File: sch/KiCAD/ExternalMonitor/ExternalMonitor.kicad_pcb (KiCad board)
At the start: 2 copper layers, 78.6 x 60.3 mm, 29 parts, among them J1 Conn_01x02_Male, J10 Conn_01x04_Female, J11 Conn_01x08_Female, J12 Conn_01x04_Female, J13 Conn_01x15, J14 Conn_01x03_Pin, J2 Conn_01x02_Male, J3 Conn_01x03_Male, J4 Conn_01x03_Male, J5 Conn_01x03_Female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

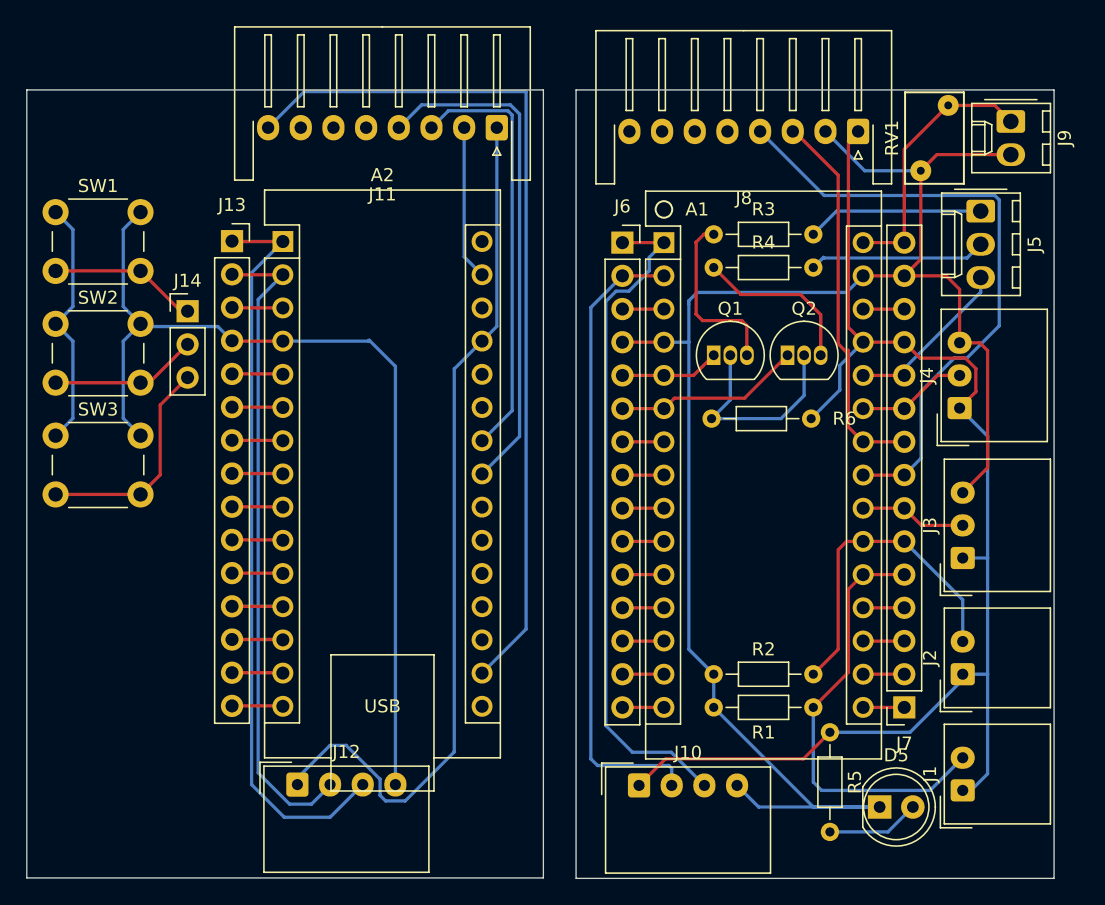
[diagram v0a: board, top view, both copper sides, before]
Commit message: 複製した回路図の重複部分を削除
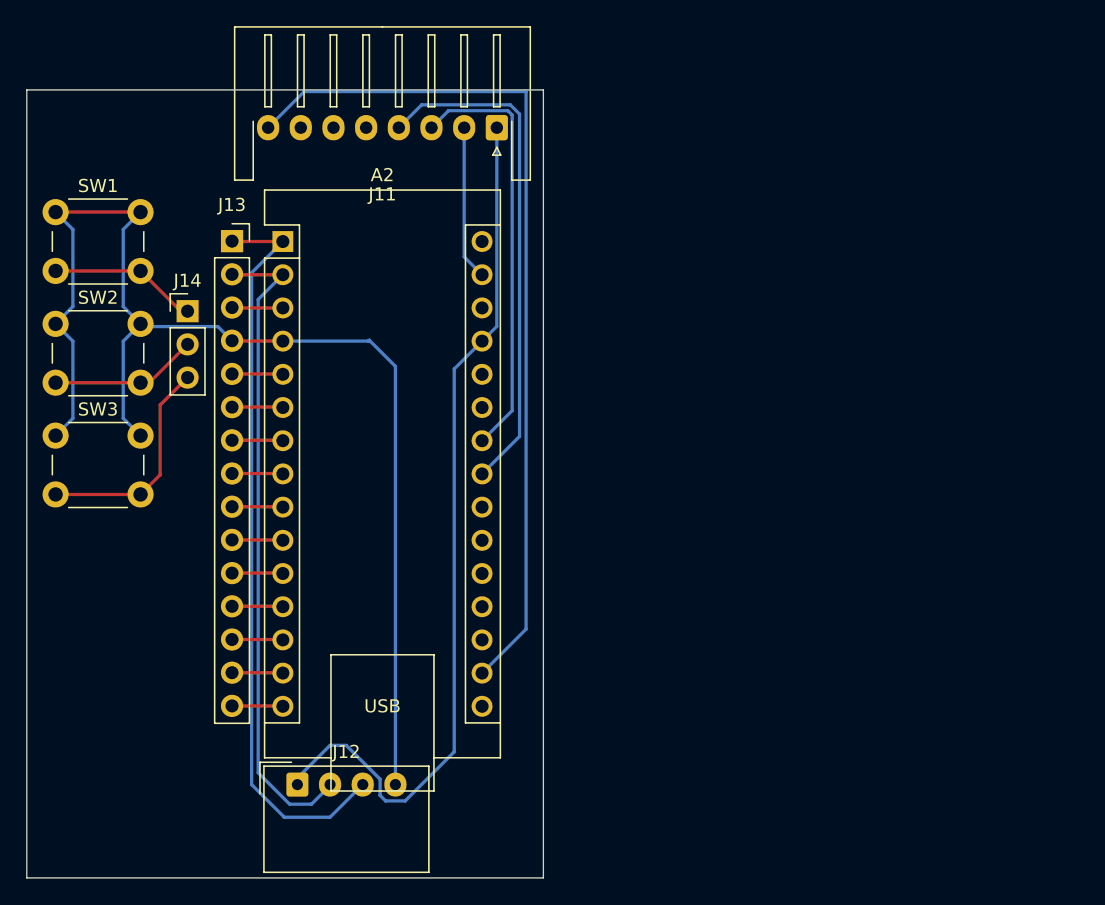
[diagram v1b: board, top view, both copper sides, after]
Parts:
- removed A1: Arduino_Nano_v3.x, Module:Arduino_Nano
- removed D5: CQY99, LED_THT:LED_D5.0mm_IRGrey
- removed J1, J2: Conn_01x02_Male, Connector_Molex:Molex_SPOX_5268-02A_1x02_P2.50mm_Horizontal
- removed J10: Conn_01x04_Female, Connector_Molex:Molex_SPOX_5268-04A_1x04_P2.50mm_Horizontal
- removed J3, J4: Conn_01x03_Male, Connector_Molex:Molex_SPOX_5268-03A_1x03_P2.50mm_Horizontal
- removed J5: Conn_01x03_Female, Connector_Molex:Molex_KK-254_AE-6410-03A_1x03_P2.54mm_Vertical
- removed J6, J7: Conn_01x15, Connector_PinSocket_2.54mm:PinSocket_1x15_P2.54mm_Vertical
- removed J8: Conn_01x08_Female, Connector_JST:JST_XH_S8B-XH-A-1_1x08_P2.50mm_Horizontal
- removed J9: Conn_01x02_Female, Connector_Molex:Molex_KK-254_AE-6410-02A_1x02_P2.54mm_Vertical
- removed Q1, Q2: 2SC1815, Package_TO_SOT_THT:TO-92_Inline
- removed R1, R2, R3, R4, R6: 10K ohm, Resistor_THT:R_Axial_DIN0204_L3.6mm_D1.6mm_P7.62mm_Horizontal
- removed R5: 200 ohm, Resistor_THT:R_Axial_DIN0204_L3.6mm_D1.6mm_P7.62mm_Horizontal
- removed RV1: RV_Disc_D7mm_W4.5mm_P5mm, Varistor:RV_Disc_D7mm_W4.5mm_P5mm
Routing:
- net +5V: track 400.2 -> 176.5 mm
- net Net-(A1-D1/TX): track 52.0 -> 0.00 mm
- net Net-(A1-D0/RX): track 48.9 -> 0.00 mm
- net Net-(A1-A4): track 48.2 -> 0.00 mm
- net Net-(A1-A1): track 33.3 -> 0.00 mm
- net Net-(A1-A5): track 29.5 -> 0.00 mm
- net Net-(A1-A2): track 25.1 -> 0.00 mm
- net +12V: track 20.3 -> 0.00 mm
- net Net-(Q1-C): track 16.8 -> 0.00 mm
- net Net-(A1-D3): track 14.3 -> 0.00 mm
- net Net-(Q1-B): track 13.6 -> 0.00 mm
- net Net-(J5-Pin_2): track 13.6 -> 0.00 mm
- net Net-(J5-Pin_1): track 13.5 -> 0.00 mm
- net Net-(A1-A7): track 13.1 -> 0.00 mm
- net Net-(Q2-B): track 12.8 -> 0.00 mm
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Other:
- board size 78.6 x 60.3 mm -> 39.5 x 60.3 mm
- board text removed: "2023/11/17"
- board text removed: "Boost"
- board text removed: "Oil.P"
- board text removed: "Oil.T"
- board text removed: "Th Sp Tc"
- board text removed: "Water"
